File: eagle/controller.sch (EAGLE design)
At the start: 32 parts, among them IC1 MAX7219CNG, IC2 ATMEGA328, IC3 LT1490AIS8, IC4 LT1490AIS8, Q1 16MHz, SW1 EC12E_SW, SW2 EC12E_SW, X1 22-23-2031, X2 22-23-2021, X3 22-23-2021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

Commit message: Remove IO parts from controller schematic and route to connector instead
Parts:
- removed IC1: MAX7219CNG, maxim:MAX7219CNG
- removed LED1, LED2: BTOF-5461AX56-12EWA, TOF-5461AG-1:BTOF-5461AX56-12EWA
- removed R1: 10k, rcl:R-EU_0207/10
- removed SW1, SW2: EC12E_SW, switch-alps:EC12E_SW
- added X5: 22-23-2101, con-molex:22-23-2101
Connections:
- removed net N$10: IC1.SEGA, LED1.A, LED2.A
- removed net N$11: IC1.SEGB, LED1.B, LED2.B
- removed net N$12: IC1.SEGC, LED1.C, LED2.C
- removed net N$13: IC1.SEGD, LED1.D, LED2.D
- removed net N$14: IC1.SEGE, LED1.E, LED2.E
- removed net N$15: IC1.SEGF, LED1.F, LED2.F
- removed net N$16: IC1.SEGG, LED1.G, LED2.G
- removed net N$17: IC1.ISET, R1.1
- removed net N$18: IC1.DIN, IC2.PB4(MISO)
- removed net N$19: IC1.CLK, IC2.PB3(MOSI/OC2)
- removed net N$20: IC1.SEGDP, LED1.DP, LED2.DP
- removed net N$4: IC1.DIG2, LED1.CA@3
- removed net N$5: IC1.DIG3, LED1.CA@4
- removed net N$6: IC1.DIG4, LED2.CA@1
- removed net N$7: IC1.DIG5, LED2.CA@2
- removed net N$8: IC1.DIG6, LED2.CA@3
- removed net N$9: IC1.DIG7, LED2.CA@4
- net GND: now also X5-10.S; no longer IC1.GND@1, IC1.GND@2, SW1G$1.C, SW1G$2.1, SW2G$1.C, SW2G$2.1
- net N$1: now also IC2.PB4(MISO), X5-9.S; no longer IC1.LOAD, IC2.PB2(SS/OC1B)
- net N$2: now also IC2.PB2(SS/OC1B), X5-8.S; no longer IC1.DIG0, LED1.CA@1
- net N$3: now also IC2.PB3(MOSI/OC2), X5-7.S; no longer IC1.DIG1, LED1.CA@2
- net N$38: now also X5-4.S; no longer SW2G$2.2
- net N$39: now also X5-1.S; no longer SW1G$2.2
- net N$40: now also X5-2.S; no longer SW1G$1.B
- net N$41: now also X5-6.S; no longer SW2G$1.A
- net N$42: now also X5-5.S; no longer SW2G$1.B
- net N$45: now also X5-3.S; no longer SW1G$1.A
- net VCC: no longer IC1.VCC, R1.2
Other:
- moved on the sheet: C3, C4, C5, C6, IC3A, IC3B, IC4A, R10, R11, R12, R5, R6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

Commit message: Finish up controller board (including pcb)
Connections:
- net VCC renamed N$4
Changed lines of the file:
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@@
 <?xml version="1.0" encoding="utf-8"?>
 <!DOCTYPE eagle SYSTEM "eagle.dtd">
-<eagle version="7.1.0">
+<eagle version="6.5.0">
 <drawing>
 <settings>
@@
 </segment>
 </net>
-<net name="VCC" class="0">
+<net name="N$4" class="0">
 <segment>
 <pinref part="IC2" gate="G$1" pin="VCC@1"/>
@@
 </segment>
 </net>
-<net name="N$39" class="0">
+<net name="N$7" class="0">
 <segment>
 <pinref part="IC2" gate="G$1" pin="PB0(ICP)"/>

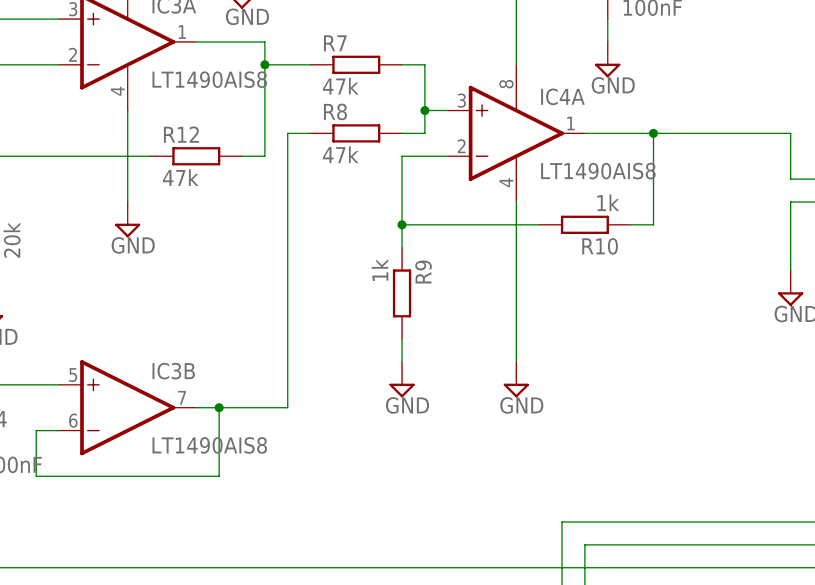
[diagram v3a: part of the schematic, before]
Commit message: Correct mistakes in the controller opamp circuit
- Coarse voltage multiplier from 5->16.75V now from 5->30V
- Summing opamp was doubling voltage, now just voltage follower
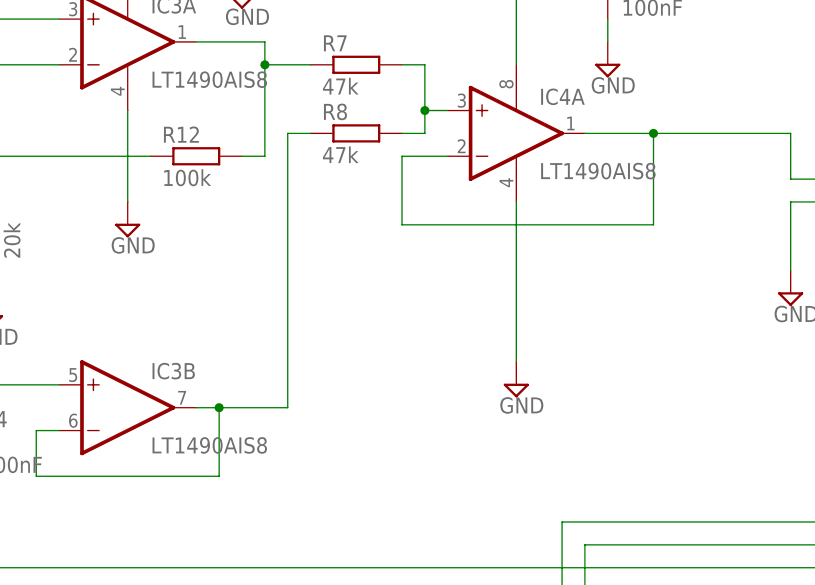
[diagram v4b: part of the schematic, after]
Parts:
- removed R10, R9: 1k, rcl:R-EU_0207/10
- R12: value 47k -> 100k
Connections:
- removed net N$37: IC4A.OUT, R10.1, X4-1.S
- net GND: no longer R9.2
- net N$36: now also IC4A.OUT, X4-1.S; no longer R10.2, R9.1
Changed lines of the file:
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@@
 <part name="R7" library="rcl" deviceset="R-EU_" device="0207/10" value="47k"/>
 <part name="R8" library="rcl" deviceset="R-EU_" device="0207/10" value="47k"/>
-<part name="R9" library="rcl" deviceset="R-EU_" device="0207/10" value="1k"/>
-<part name="R10" library="rcl" deviceset="R-EU_" device="0207/10" value="1k"/>
-<part name="SUPPLY10" library="supply2" deviceset="GND" device=""/>
 <part name="R11" library="rcl" deviceset="R-EU_" device="0207/10" value="20k"/>
-<part name="R12" library="rcl" deviceset="R-EU_" device="0207/10" value="47k"/>
+<part name="R12" library="rcl" deviceset="R-EU_" device="0207/10" value="100k"/>
 <part name="SUPPLY11" library="supply2" deviceset="GND" device=""/>
 <part name="X4" library="con-molex" deviceset="22-23-2021" device=""/>
@@
 <instance part="R7" gate="G$1" x="213.36" y="121.92"/>
 <instance part="R8" gate="G$1" x="213.36" y="114.3"/>
-<instance part="R9" gate="G$1" x="218.44" y="96.52" rot="R270"/>
-<instance part="R10" gate="G$1" x="238.76" y="104.14" rot="R180"/>
-<instance part="SUPPLY10" gate="GND" x="218.44" y="86.36"/>
 <instance part="R11" gate="G$1" x="172.72" y="104.14" rot="R90"/>
 <instance part="R12" gate="G$1" x="195.58" y="111.76"/>
@@
 </segment>
 <segment>
-<pinref part="R9" gate="G$1" pin="2"/>
-<pinref part="SUPPLY10" gate="GND" pin="GND"/>
-<wire x1="218.44" y1="91.44" x2="218.44" y2="88.9" width="0.1524" layer="91"/>
-</segment>
-<segment>
 <pinref part="R11" gate="G$1" pin="1"/>
 <pinref part="SUPPLY11" gate="GND" pin="GND"/>
@@
 <net name="N$36" class="0">
 <segment>
-<pinref part="R9" gate="G$1" pin="1"/>
-<wire x1="218.44" y1="101.6" x2="218.44" y2="104.14" width="0.1524" layer="91"/>
 <pinref part="IC4" gate="A" pin="-IN"/>
 <wire x1="218.44" y1="104.14" x2="218.44" y2="111.76" width="0.1524" layer="91"/>
 <wire x1="218.44" y1="111.76" x2="223.52" y2="111.76" width="0.1524" layer="91"/>
-<pinref part="R10" gate="G$1" pin="2"/>
-<wire x1="233.68" y1="104.14" x2="218.44" y2="104.14" width="0.1524" layer="91"/>
-<junction x="218.44" y="104.14"/>
-</segment>
-</net>
-<net name="N$37" class="0">
-<segment>
-<pinref part="R10" gate="G$1" pin="1"/>
-<wire x1="243.84" y1="104.14" x2="246.38" y2="104.14" width="0.1524" layer="91"/>
+<wire x1="246.38" y1="104.14" x2="218.44" y2="104.14" width="0.1524" layer="91"/>
 <wire x1="246.38" y1="104.14" x2="246.38" y2="114.3" width="0.1524" layer="91"/>
 <pinref part="IC4" gate="A" pin="OUT"/>

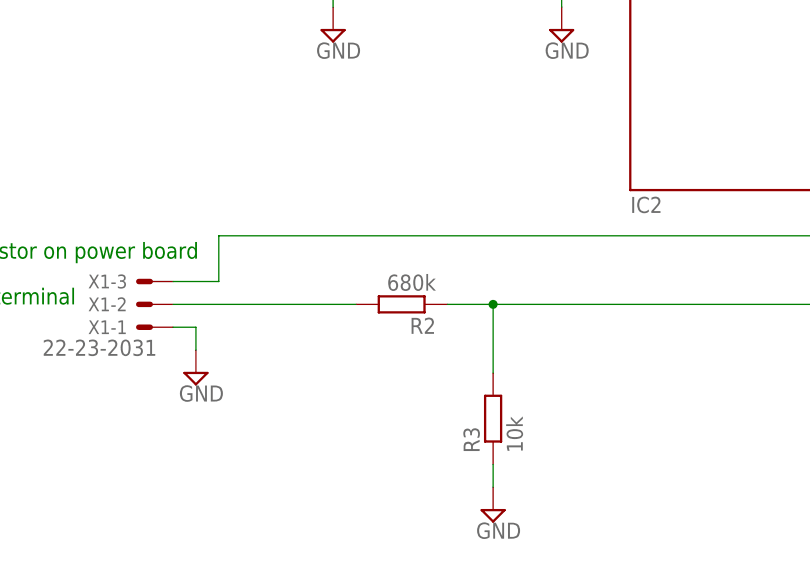
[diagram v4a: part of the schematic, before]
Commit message: Correct another mistake in controller board
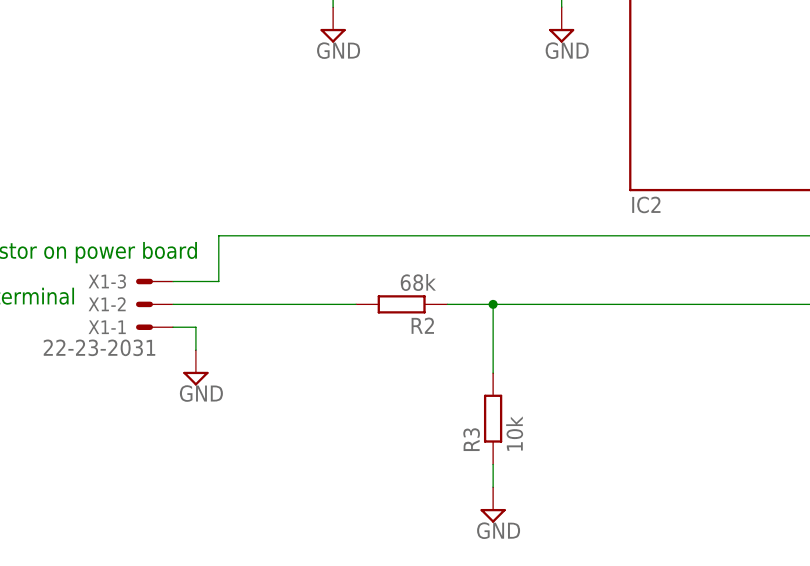
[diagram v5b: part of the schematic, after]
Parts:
- R2: value 680k -> 68k
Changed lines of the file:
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@@
 <part name="P+2" library="supply1" deviceset="VCC" device=""/>
 <part name="SUPPLY2" library="supply2" deviceset="GND" device=""/>
-<part name="R2" library="rcl" deviceset="R-EU_" device="0207/10" value="680k"/>
+<part name="R2" library="rcl" deviceset="R-EU_" device="0207/10" value="68k"/>
 <part name="R3" library="rcl" deviceset="R-EU_" device="0207/10" value="10k"/>
 <part name="SUPPLY3" library="supply2" deviceset="GND" device=""/>
